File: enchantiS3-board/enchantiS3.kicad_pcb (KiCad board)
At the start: 4 copper layers, 55.9 x 25.4 mm, 54 parts, among them J1 USB_C_Receptacle_USB2.0, SW1 BOOT, SW2 ESP_RST, SW3 SYS_RST, U1 USBLC6-2P6, U2 NCP187, U3 ICM-42670-P, U7 NPM1300-QEAA-R7, U8 MMC5983MA

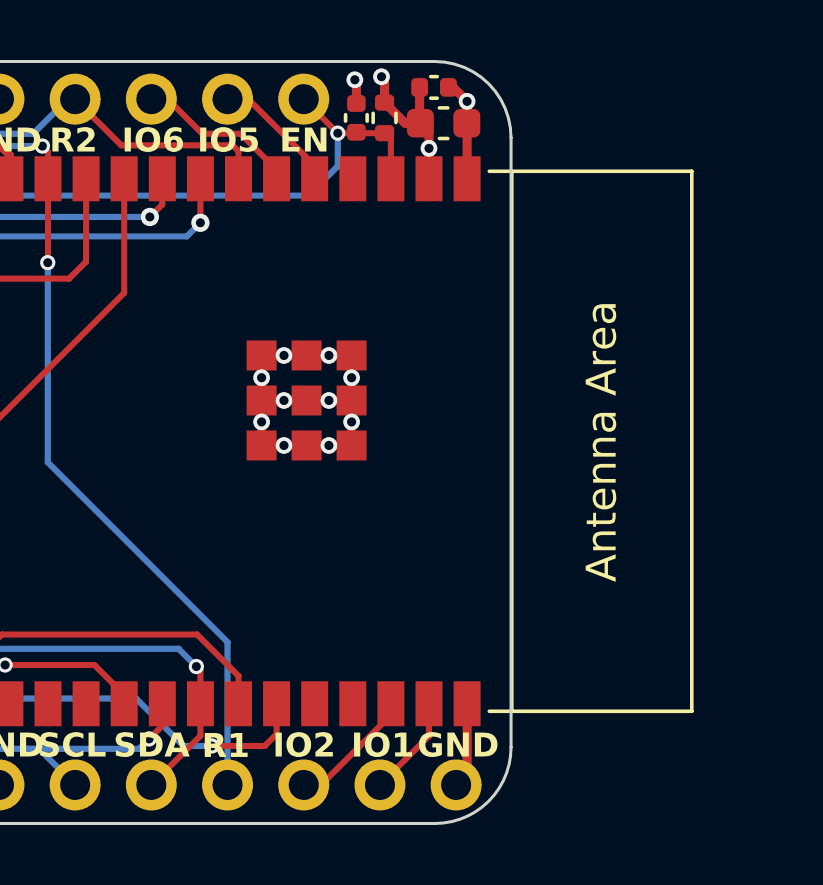
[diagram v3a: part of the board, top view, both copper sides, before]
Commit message: Switch to cheaper ESP32S3 WROOM 1 N8R8 Module
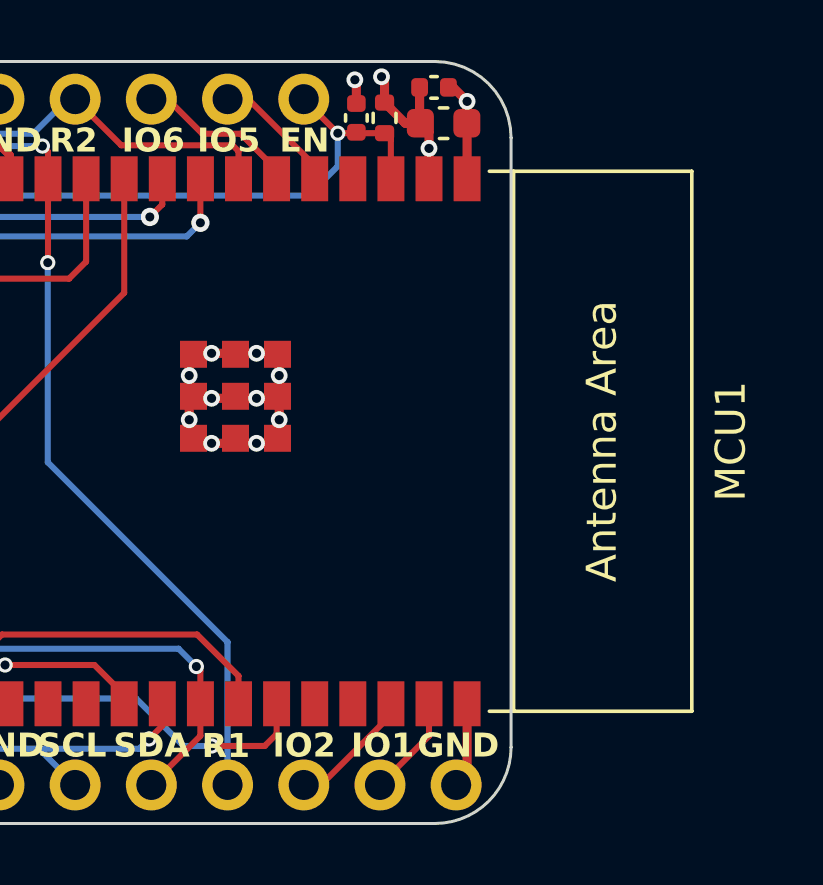
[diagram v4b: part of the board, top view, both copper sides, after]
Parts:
- MCU1: value ESP32-S3-WROOM-2 -> ESP32-S3-WROOM-1; footprint PCM_Espressif:ESP32-S3-WROOM-2 -> PCM_Espressif:ESP32-S3-WROOM-1
